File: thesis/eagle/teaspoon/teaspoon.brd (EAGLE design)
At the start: 63.2 x 73 mm, 23 parts, among them IC1 7805DT, IC2 7805DT, U1 ADCS7477

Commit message: didn't do anything here
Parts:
- moved C1 1.27 mm to (75.6, 41.3)
- moved C2 1.27 mm to (75.6, 36.2)
- moved C3 1.27 mm to (72.4, 34.9)
- moved C4 1.27 mm to (72.4, 43.8)
- moved IC1 1.27 mm to (80.6, 61.6)
- moved IC2 1.27 mm to (68.6, 39.4)
- moved M1 1.27 mm to (96.5, 54.6)
- moved M2 1.27 mm to (99.1, 52.7)
- moved M4 1.27 mm to (99.1, 47.6)
- moved M7 1.27 mm to (96.5, 39.4)
- moved C5 1.27 mm to (85.7, 58.4)
- moved C6 1.27 mm to (88.3, 58.4)
- moved C7 1.27 mm to (74.9, 58.4)
- moved C8 1.27 mm to (72.4, 58.4)
- moved JP1 1.27 mm to (92.1, 35.6)
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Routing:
- net N$5: track 72.7 -> 75.0 mm
- net SE: track 54.5 -> 56.7 mm
- net !CS: track 18.3 -> 19.6 mm
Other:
- board size 63.2 x 73 mm -> 108.3 x 73 mm

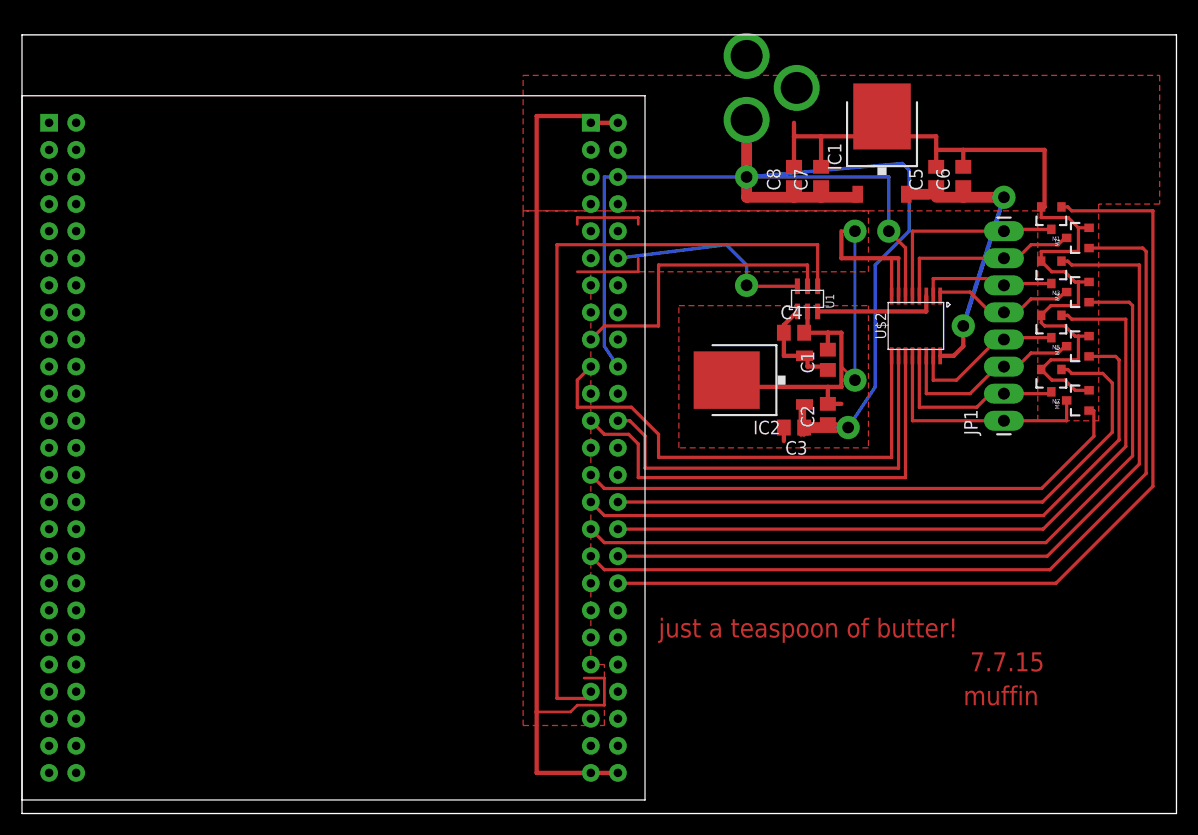
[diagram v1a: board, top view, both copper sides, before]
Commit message: moved the dimension over .01 inch
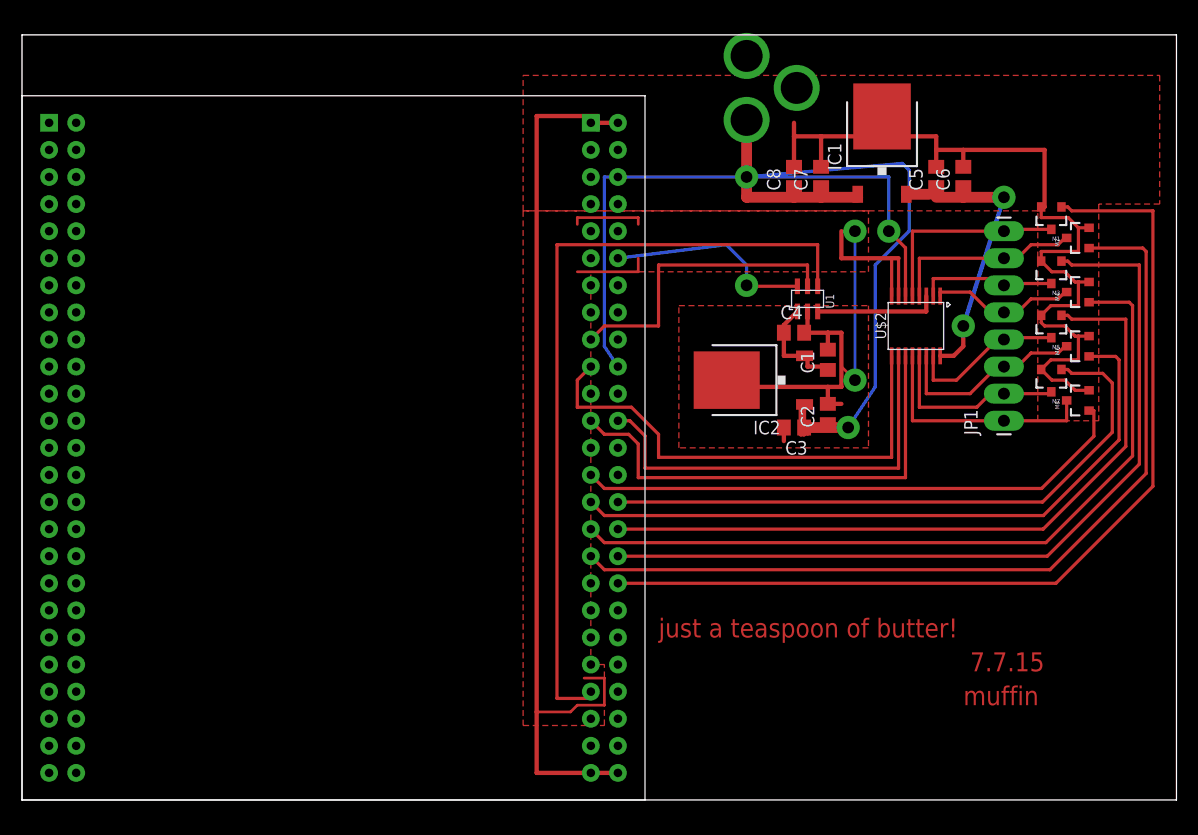
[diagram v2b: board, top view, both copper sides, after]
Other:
- board size 108.3 x 73 mm -> 108.3 x 71.7 mm
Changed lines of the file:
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@@
 <board>
 <plain>
-<wire x1="0" y1="-1.27" x2="108.255" y2="-1.27" width="0" layer="20"/>
-<wire x1="108.255" y1="-1.27" x2="108.255" y2="71.745" width="0" layer="20"/>
+<wire x1="0" y1="0" x2="108.255" y2="0" width="0" layer="20"/>
+<wire x1="108.255" y1="0" x2="108.255" y2="71.745" width="0" layer="20"/>
 <wire x1="108.255" y1="71.745" x2="0" y2="71.745" width="0" layer="20"/>
-<wire x1="0" y1="71.745" x2="0" y2="-1.27" width="0" layer="20"/>
+<wire x1="0" y1="71.745" x2="0" y2="0" width="0" layer="20"/>
 <text x="59.69" y="15.24" size="1.778" layer="1">just a teaspoon of butter!</text>
 <text x="88.9" y="12.065" size="1.778" layer="1">7.7.15</text>
